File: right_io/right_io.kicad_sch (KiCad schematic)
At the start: 0 parts

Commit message: Board split Phase 2.4: trim center board, FPC boundary contracts, per-project verification
Center (ducktop2) loses the four sheets that moved to the daughterboards:
04_usb_c_io, 05_power_inputs, 06_tcp0_external_hdmi, 16_gigabit_ethernet,
and the pack-protection section of 01_power_battery (BMS board). J190 AUX
terminal moves to the left board. Center keeps 9 sheets: charger/gauge/
ship-FET (U2/U10/Q25/RS1), EC, Mu, radio, internal, radio-DB, keyboard x2,
maker, audio. 717 components.

FPC-1/2/3 boundary contracts declare the crossing nets at the center root
(30 + 35 + 4 shared nets; HUB_DS1_DP/DM are center pass-throughs).

Verification is now per-project:
- verify_design_contracts.py --project {ducktop2,left_io,right_io,bms}
  (five-port USB-C contracts split by port, HDMI/GbE run on right_io,
  pack contracts run on bms, sheet names parameterized)
- verify_schematic_closure.py --pack audits the BMS pack block
- verify_electrical_calculations.py --project bms for pack calcs
- pin review trimmed to center parts; FPC-boundary nets in ERC allowlist

Fixed while trimming: daughterboard root labels now sit on sheet-block pin
endpoints (left/right FPC nets actually connect); duplicate GND pwrflag in
power sheet; sync.parse_netlist respects the radio-daughterboard override.

Schematic gate PASS: self-check, closure audits (89+151), electrical
calcs (67+15), pin review (1625), identity.
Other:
- sheet GbE ports: added none; removed HUB_DS1_DM, HUB_DS1_DP, MCU_3V3, MU_HOST_ACTIVE, PD2_EFUSE_FAULT_N, PD2_I2C_SCL, PD2_I2C_SDA, PD2_PATH_EN, PD2_TCPC_IRQ_N, PD2_VBUS_RAW, PD_PROTECT_FAULT_N, SYS_3V3, SYS_5V, TCP0_DDC_SCL, TCP0_DDC_SDA, TCP0_HPD, TCP0_TX0_N, TCP0_TX0_P, TCP0_TX1_N, TCP0_TX1_P, TCP0_TXRX0_N, TCP0_TXRX0_P, TCP0_TXRX1_N, TCP0_TXRX1_P, USB_PORT_5V
- sheet HDMI ports: added none; removed GBE_CLKREQ_N, GBE_HOST_RX_N, GBE_HOST_RX_P, GBE_HOST_TX_N, GBE_HOST_TX_P, GBE_REFCLK_N, GBE_REFCLK_P, HUB_DS1_DM, HUB_DS1_DP, MCU_3V3, PCIE_3V3, PCIE_WAKE_N, PD2_EFUSE_FAULT_N, PD2_I2C_SCL, PD2_I2C_SDA, PD2_PATH_EN, PD2_TCPC_IRQ_N, PD2_VBUS_RAW, PD_PROTECT_FAULT_N, PLTRST_SRC_N, USB_PORT_5V
- sheet PD2 Dual-Role ports: added none; removed GBE_CLKREQ_N, GBE_HOST_RX_N, GBE_HOST_RX_P, GBE_HOST_TX_N, GBE_HOST_TX_P, GBE_REFCLK_N, GBE_REFCLK_P, MU_HOST_ACTIVE, PCIE_3V3, PCIE_WAKE_N, PLTRST_SRC_N, SYS_5V, TCP0_DDC_SCL, TCP0_DDC_SDA, TCP0_HPD, TCP0_TX0_N, TCP0_TX0_P, TCP0_TX1_N, TCP0_TX1_P, TCP0_TXRX0_N, TCP0_TXRX0_P, TCP0_TXRX1_N, TCP0_TXRX1_P

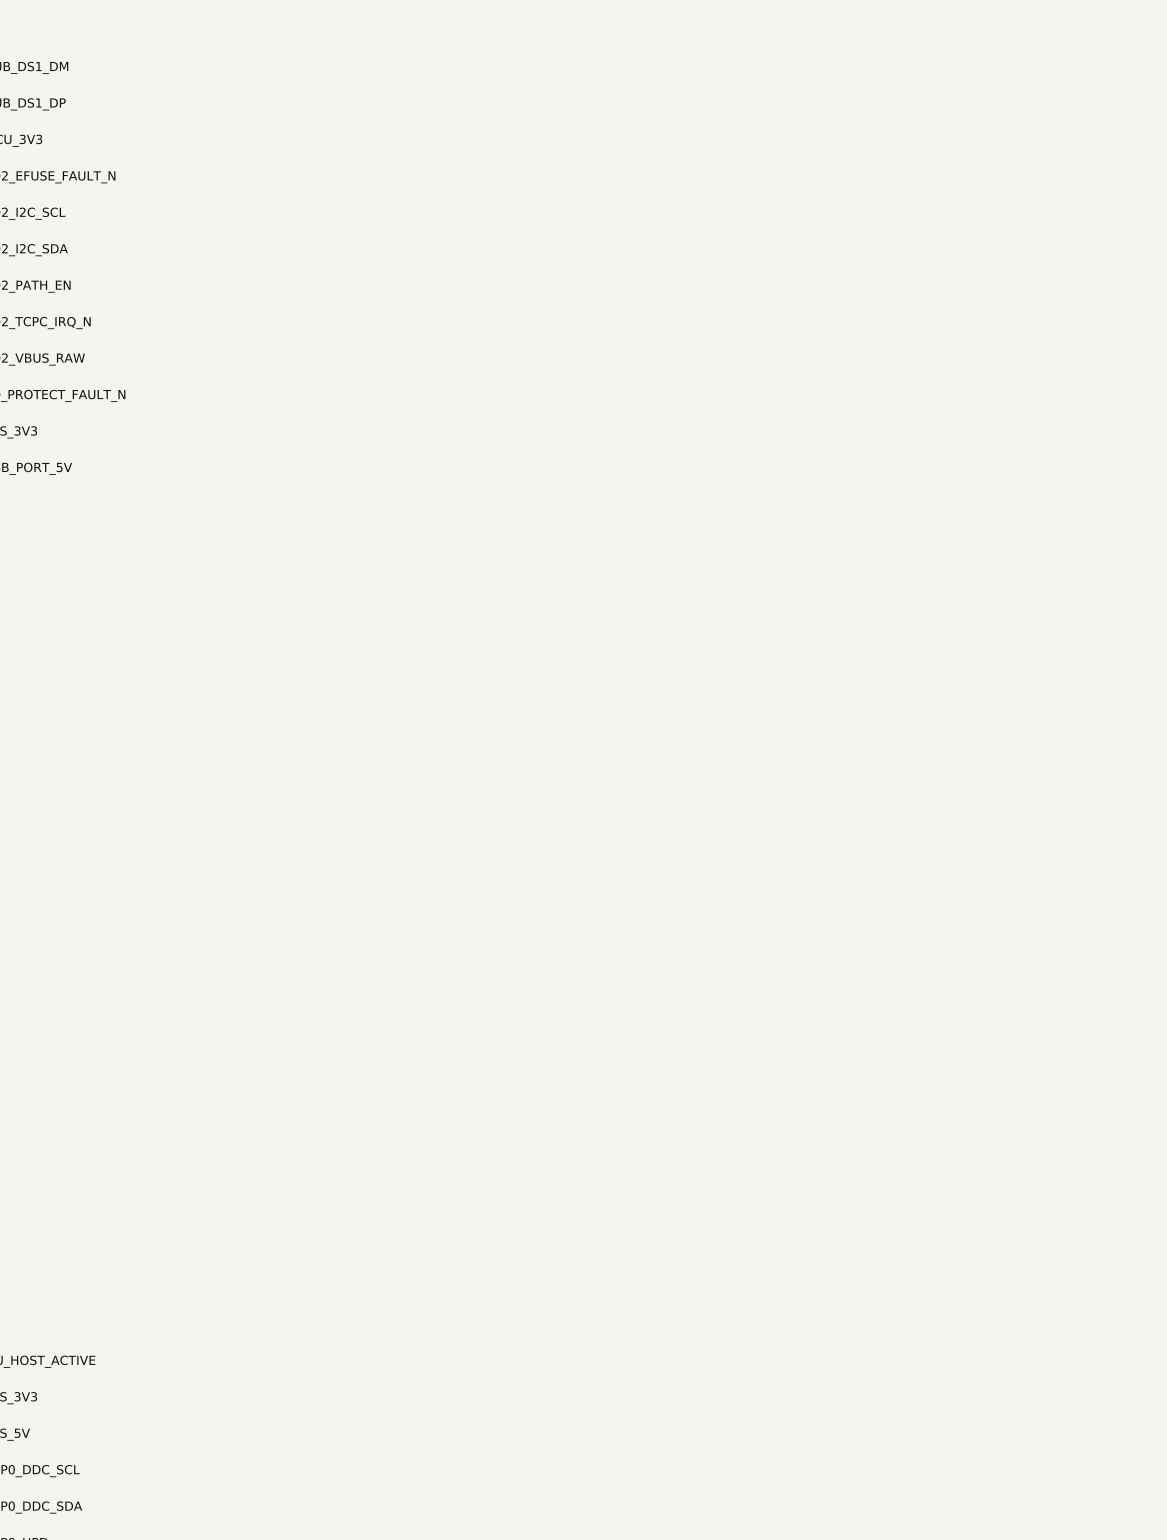
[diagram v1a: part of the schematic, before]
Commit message: Board split Phase 4a: FPC connectors wired through the four split schematics
Connector symbols and sheets now exist in every project and the boundary
nets are pinned through them (same conductor order on both ends, verified
netlist-by-netlist):
  - gen/fpc_contract.py: authoritative FPC-1/2/3 pin maps + center-side
    renames (single source of truth for schematics, board pad nets, cable
    spec, and gate contracts)
  - gen/Conn_01x100_FFC_MP.kicad_sym (derived from the 30-pin pattern)
  - center: real fpc1_left/fpc2_right/fpc3_bms sheets wired to host pins
  - left_io/right_io: left_fpc/right_fpc connector sheets; bms carries
    FPC106 inline
  - connector refs FPC101..FPC106 (valid designators; FPC1_L-style refs
    broke KiCad annotation)
  - pack-rail naming reconciled: center gauge divider BAT_PROT_VIN ->
    PACK_POS_FUSED (same node as the BMS LTC4368 output); BMS ground
    /GND -> GND (pack negative is the system ground)

Boards: daughterboards re-synced from their connector-bearing schematics;
center connectors placed and their pad nets assigned text-side ((net
"name") convention).  Connector pads verified against every other
footprint (0 overlaps) and DRC shows 0 shorts on all four boards (center
16 pre-existing, down from 17).

Fixed two latent generator bugs exposed by the wiring:
  - resolve_connectors used naive +R rotation, placing Phase 3 connectors
    against mirrored phantom positions
  - pad half-extents were computed as footprint_rot+pad_rot, but KiCad
    saves pads with world orientation (FH12-100S pins are 1.3mm wide);
    both verified empirically against pcbnew, plus a connector-nudge pass
    for parts sandwiched between the connector body and pin columns

Gate: SCHEMATIC RELEASE CHECK: PASS (FPC pin contracts added per project;
closure audits 0 FAIL).  Routing remains manual (Phase 4b).
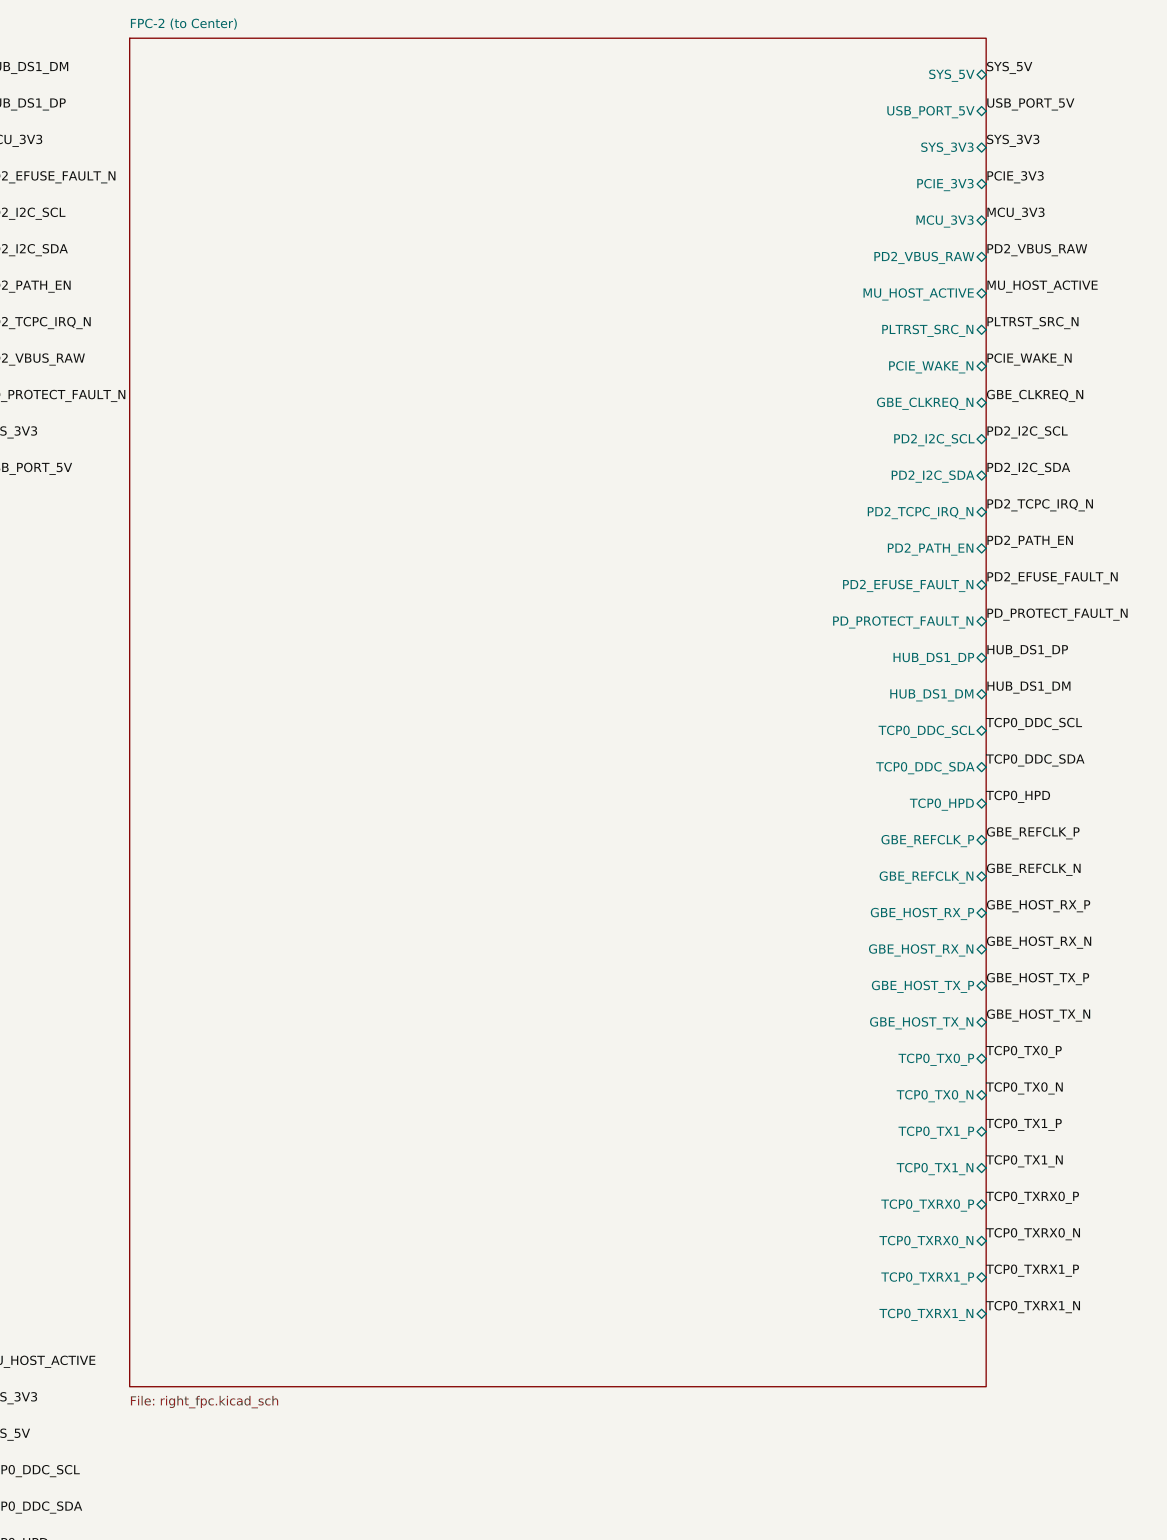
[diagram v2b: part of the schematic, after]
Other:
- added sheet FPC-2 (to Center) (right_fpc.kicad_sch)

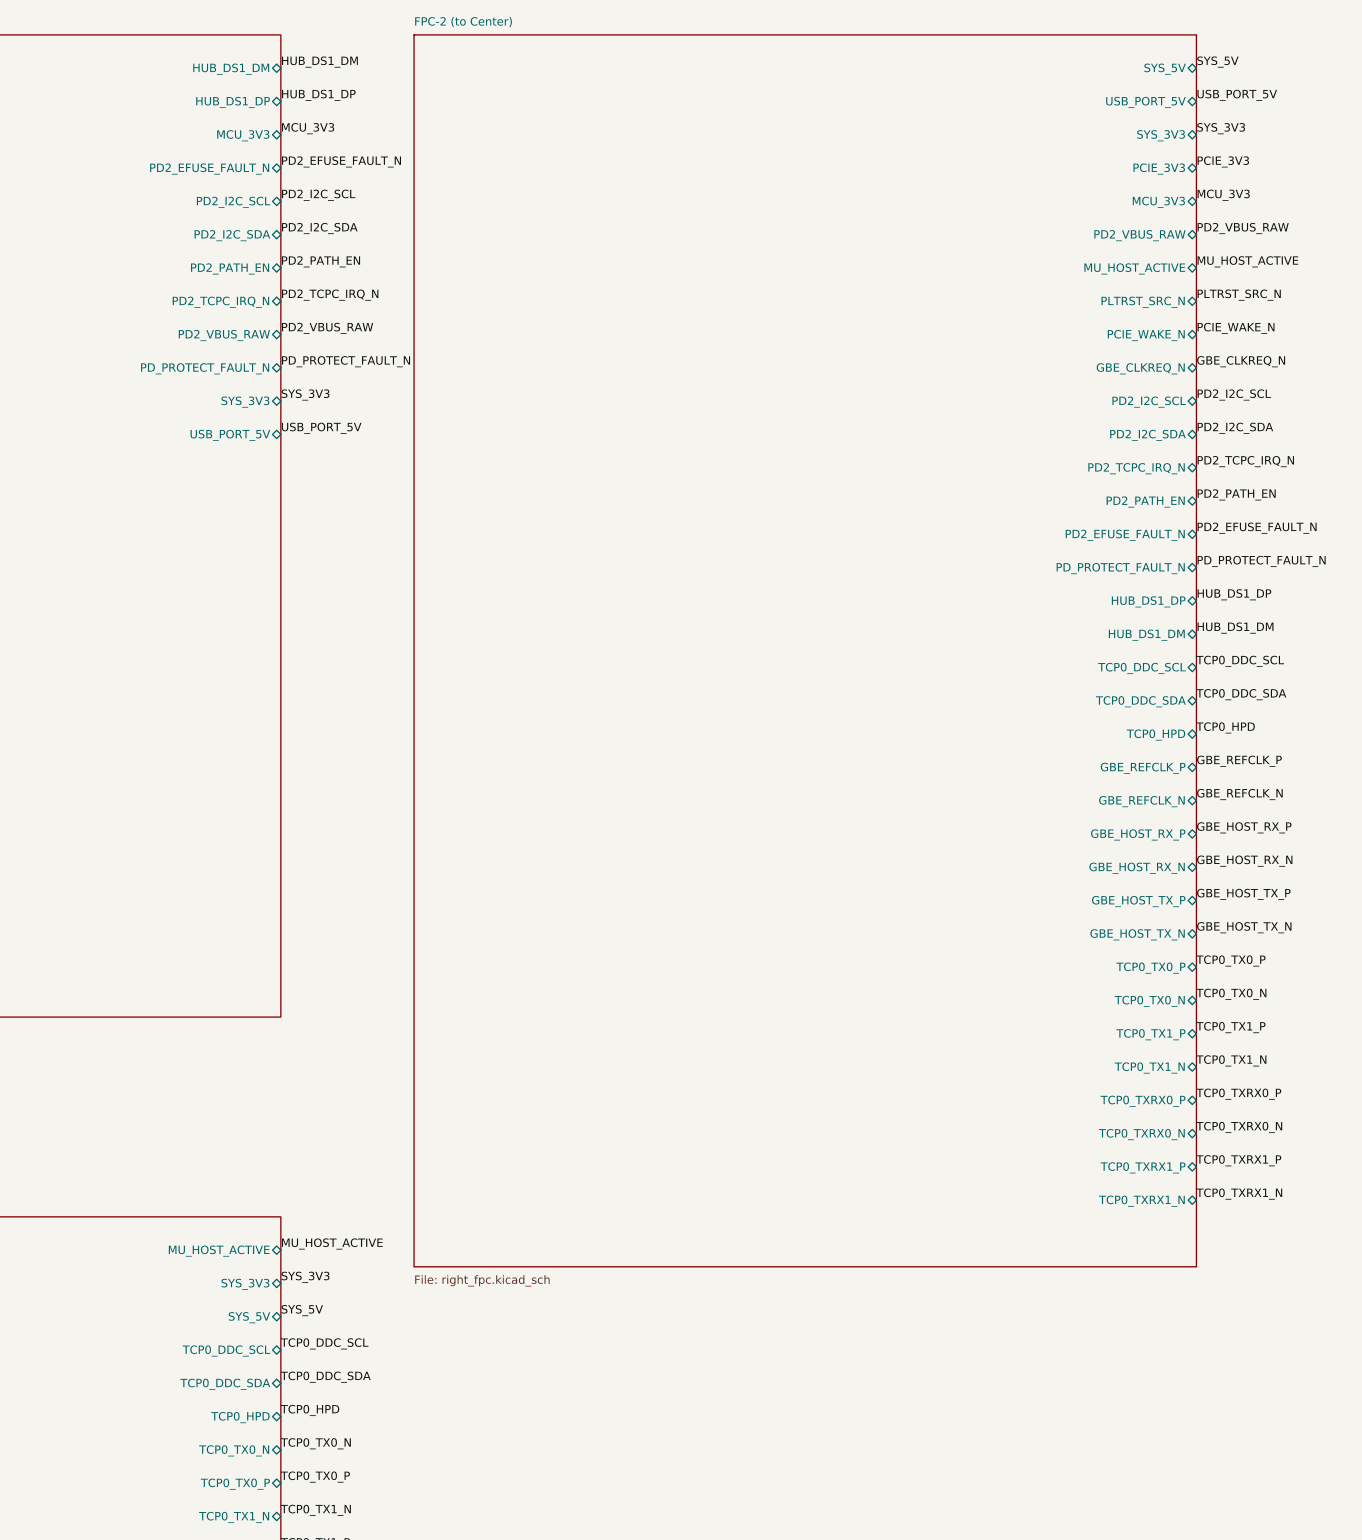
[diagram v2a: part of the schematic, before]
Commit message: Phase 5: second-opinion audit remediation + rebuilt, verified board pipeline
Second-opinion AI audit found A-tier defects; remediation applied and the
board pipeline rebuilt on a known-good base with the fixes it needed:

- electrical: LTC4418IUF symbol pinout corrected (both selectors were
  dead as drawn); center charge cascade (U15 <- U15B, PD1 > PD2 > AUX);
  pack negative never crosses FPC-3, 15-pin FG_VSS return; power-budgeted
  FPC pin maps (0.4 A/pin derate); J12/DS4 completed; AUX source fuse
- FH41-68S footprint: 13 datasheet-correct SH pads + SH pin in symbol
- connector geometry settled against the Hirose FH12 2D drawing: FFC
  enters opposite the solder pins (mouth = local +Y); reversed side-B
  maps are correct for the 180-deg-mounted pairs; rotations set so mouths
  face across every seam
- pipeline (generate_split_boards.py): per-pin pad-net resync from the
  netlists (kills shadow nets for good), netlist-exact name
  normalization, netlist-only part injection (cascade, probe headers),
  zone refill after outline swap, read-before-write race fixed, orphan
  parts dropped loudly, non-zero exit on unresolved overlaps
- monolith board relocated to old/monolith_ducktop2.kicad_pcb (placement
  oracle for the center cut only)

verified end state: 4 boards 0 shorts / 0 clearance / 0 drill, 0 boundary
crossings, 6/6 connectors contract-exact with mouths facing, 0 shadow
nets, gates PASS x4, ERC 0 x4. routing next (499 nets/board).
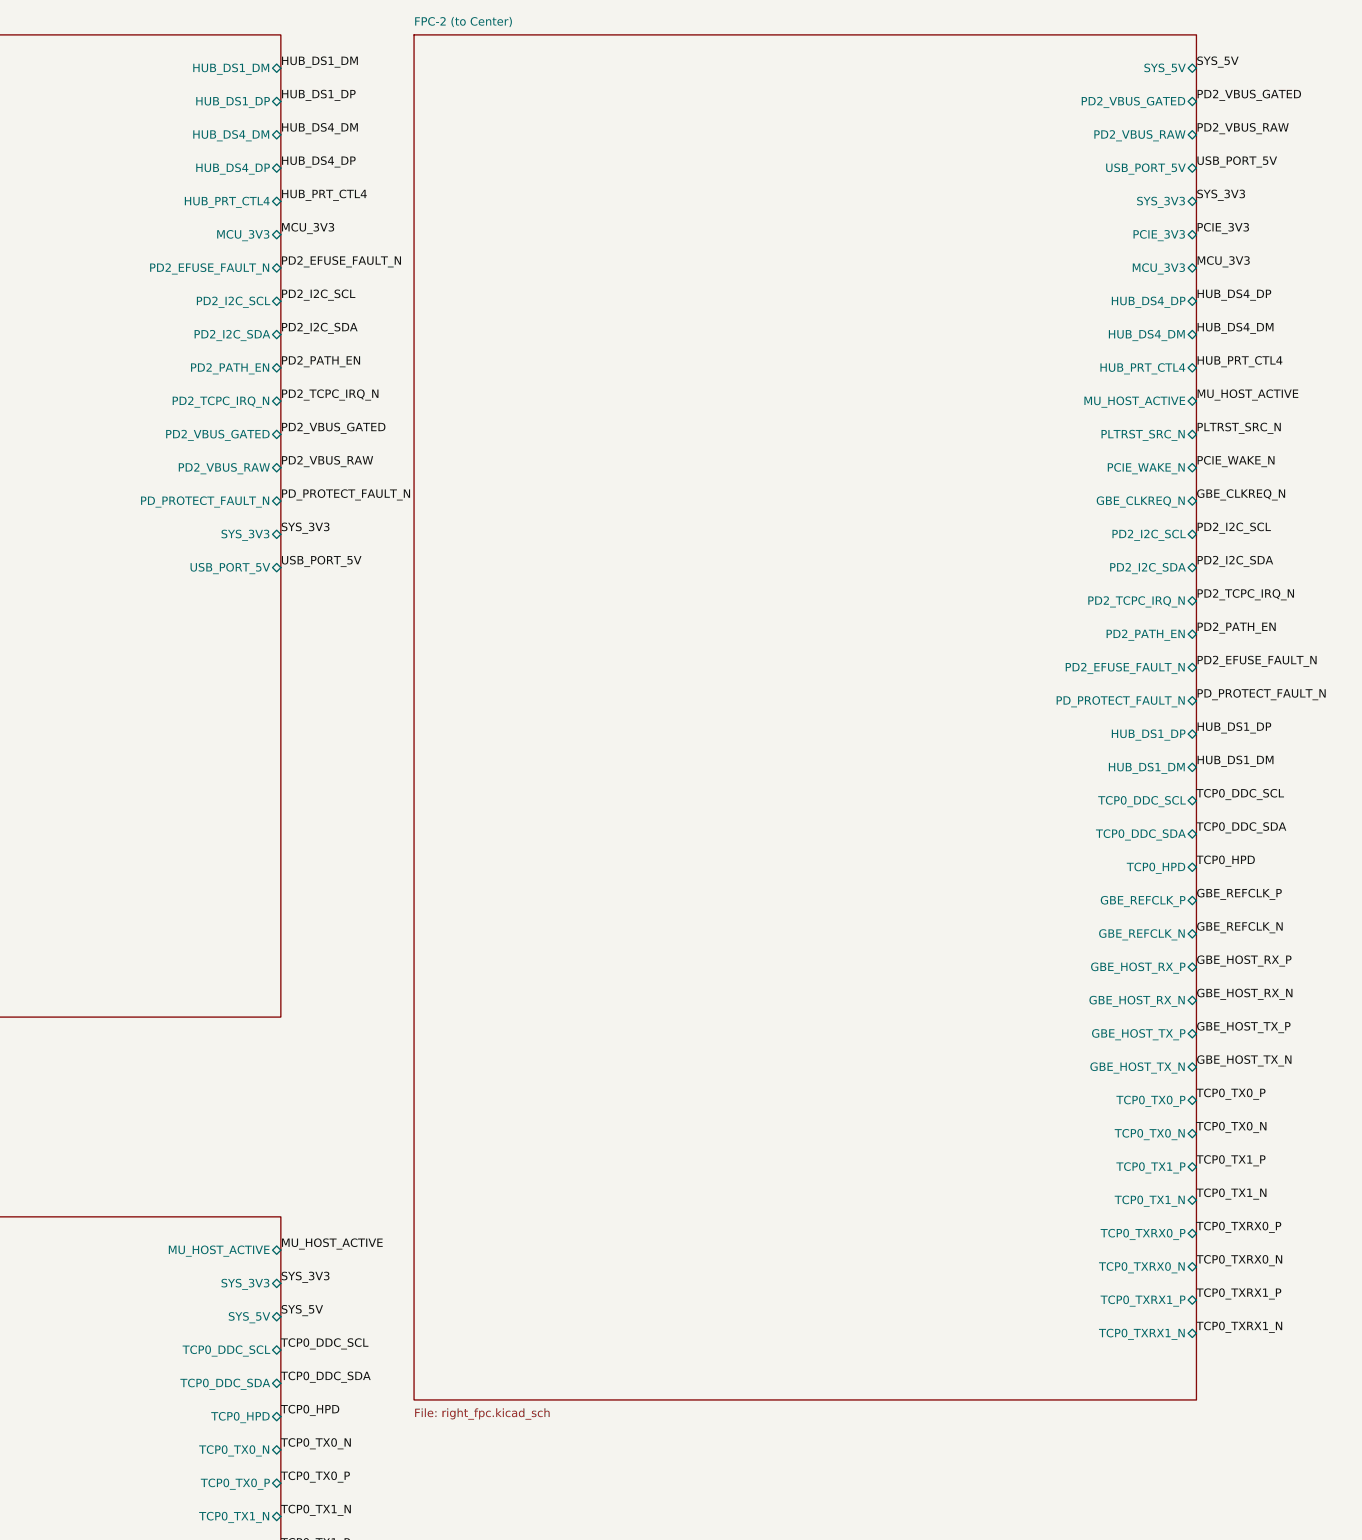
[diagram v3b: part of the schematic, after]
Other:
- sheet FPC-2 (to Center) ports: added HUB_DS4_DM, HUB_DS4_DP, HUB_PRT_CTL4, PD2_VBUS_GATED; removed none
- sheet PD2 Dual-Role ports: added HUB_DS4_DM, HUB_DS4_DP, HUB_PRT_CTL4, PD2_VBUS_GATED; removed none
